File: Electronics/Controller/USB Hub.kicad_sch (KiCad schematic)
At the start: 4 parts, among them J14 MASTER TABLET

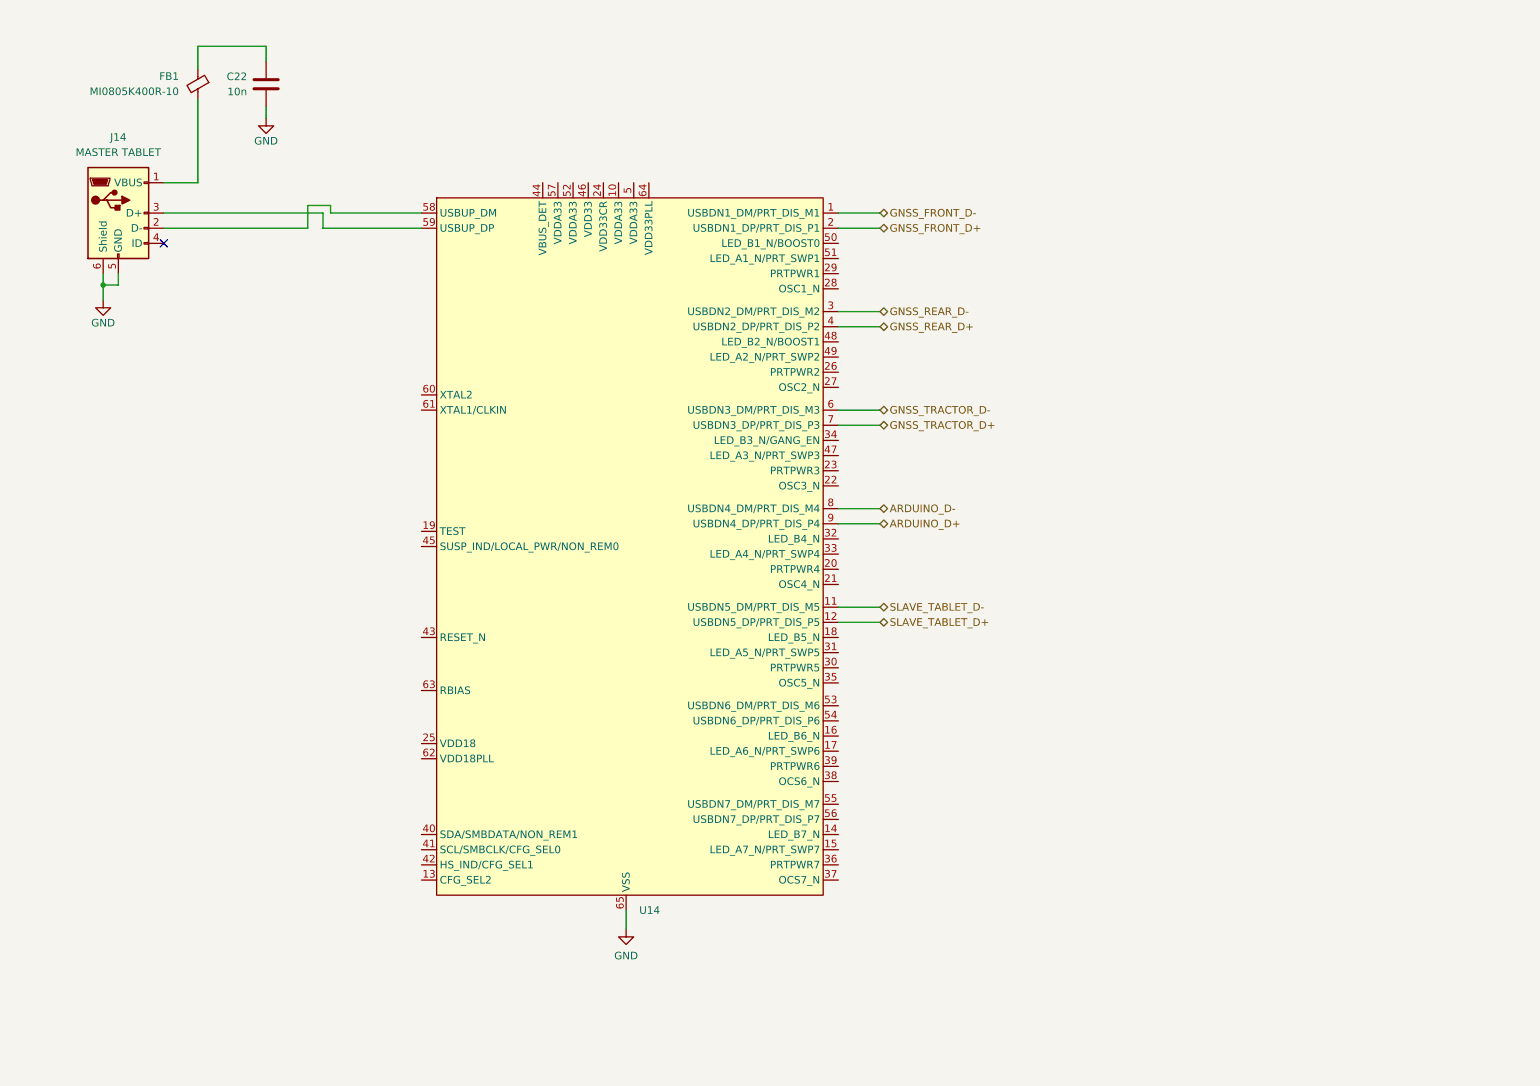
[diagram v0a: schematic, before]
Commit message: Working on schematic. Added datasheets.
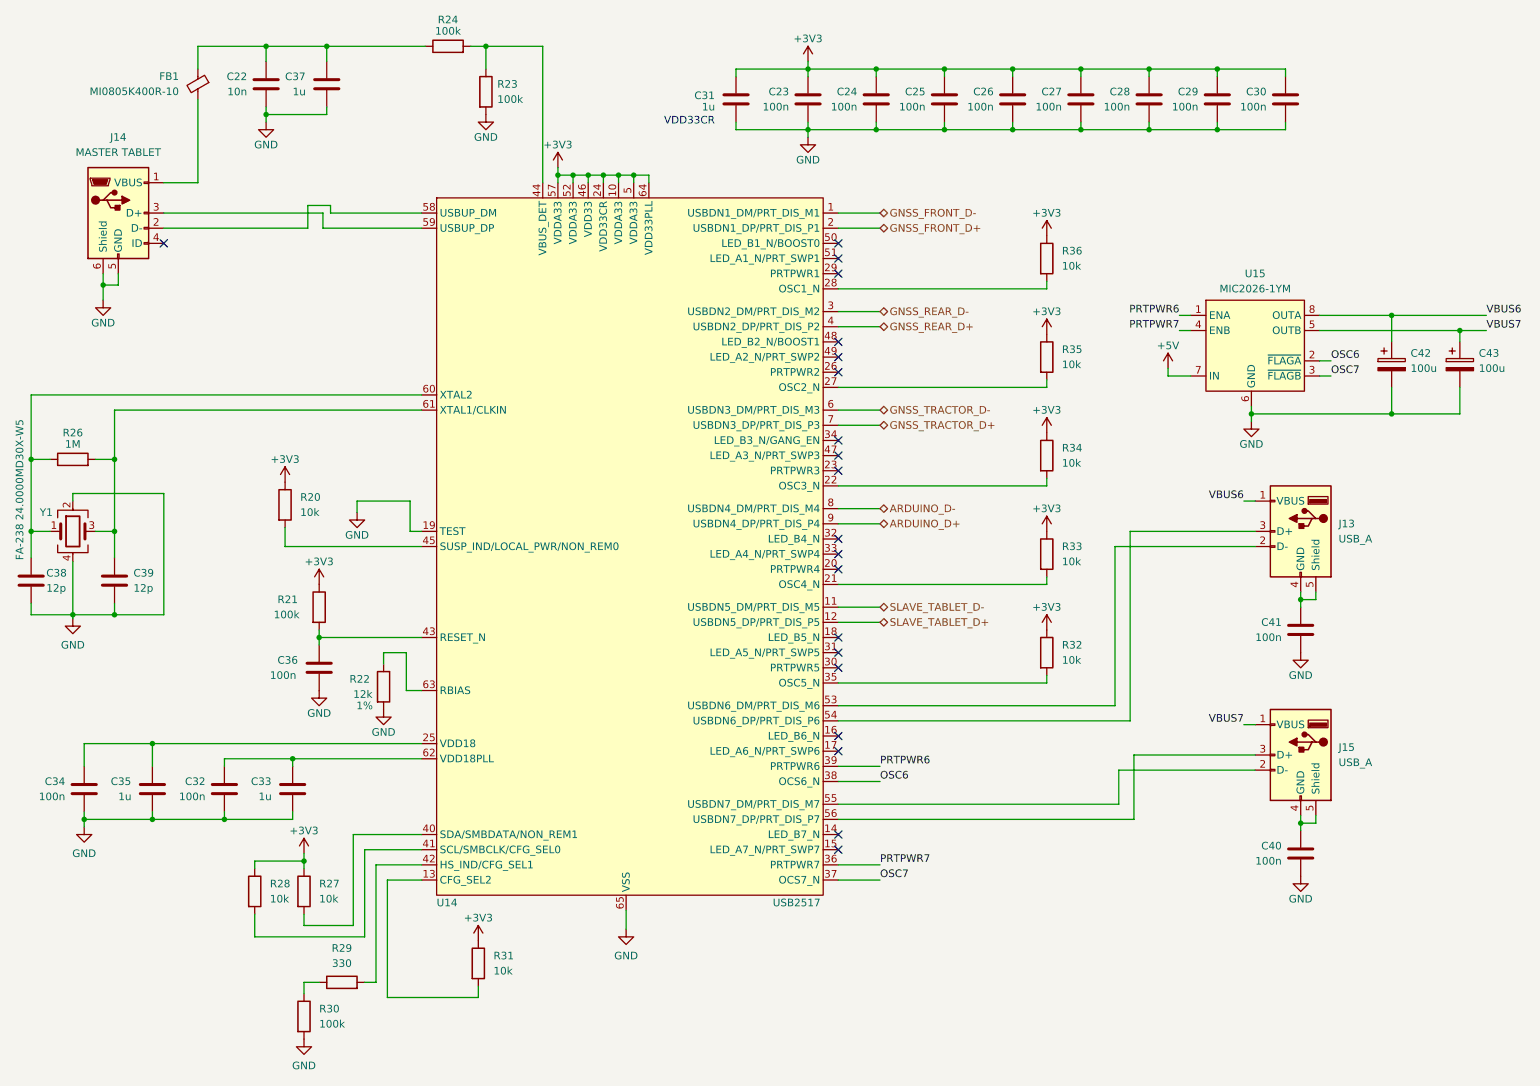
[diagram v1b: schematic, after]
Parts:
- added C23, C24, C25, C26, C27, C28, C29, C30, C32, C34, C36, C40, C41: 100n, symbol Device:C
- added C31, C33, C35, C37: 1u, symbol Device:C
- added C38, C39: 12p, symbol Device:C
- added C42, C43: 100u, symbol Device:C_Polarized
- added J13, J15: USB_A, symbol Connector:USB_A
- added R20, R27, R28, R31, R32, R33, R34, R35, R36: 10k, symbol Device:R
- added R21, R23, R24, R30: 100k, symbol Device:R
- added R22: 12k, symbol Device:R
- added R26: 1M, symbol Device:R
- added R29: 330, symbol Device:R
- added U15: MIC2026-1YM, Package_SO:SOIC-8_3.9x4.9mm_P1.27mm, symbol BritishIdeas2:MIC2026-1YM
- added Y1: FA-238 24.0000MD30X-W5, EmSA:FA-238, symbol Device:Crystal_GND24
- U14: value ~ -> USB2517
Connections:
- net GND: now also U14.19 (TEST), C23.2, C24.2, C25.2, C26.2, C27.2, C28.2, C29.2, C30.2, C31.2, C32.2, C33.2, C34.2, C35.2, C36.2, C37.2, C38.2, C39.2, C40.2, C41.2, C42.2, C43.2, R22.2, R23.2, R30.2, U15.6 (GND), Y1.2, Y1.4
- net at C22.1, FB1.1: now also C37.1, R24.1
- net +3V3: now reaches U14.10 (VDDA33)
- net +3V3: now also U14.24 (VDD33CR), U14.46 (VDD33), U14.5 (VDDA33), U14.52 (VDDA33), U14.57 (VDDA33), U14.64 (VDD33PLL), C23.1, C24.1, C25.1, C26.1, C27.1, C28.1, C29.1, C30.1, C31.1, R20.1, R21.1, R27.1, R28.1, R31.1, R32.1, R33.1, R34.1, R35.1, R36.1
- net at U14.13 (CFG_SEL2): now also R31.2
- net at U14.21 (OSC4_N): now also R33.2
- net at U14.22 (OSC3_N): now also R34.2
- net at U14.25 (VDD18): now also C34.1, C35.1
- net at U14.27 (OSC2_N): now also R35.2
- net at U14.28 (OSC1_N): now also R36.2
- net at U14.35 (OSC5_N): now also R32.2
- net PRTPWR7: now reaches U14.36 (PRTPWR7)
- net PRTPWR7: now also U15.4 (ENB)
- net OSC7: now reaches U14.37 (OCS7_N)
- net OSC7: now also U15.3 (~{FLAGB})
- net OSC6: now reaches U14.38 (OCS6_N)
- net OSC6: now also U15.2 (~{FLAGA})
- net PRTPWR6: now reaches U14.39 (PRTPWR6)
- net PRTPWR6: now also U15.1 (ENA)
- net at U14.40 (SDA/SMBDATA/NON_REM1): now also R27.2
- net at U14.41 (SCL/SMBCLK/CFG_SEL0): now also R28.2
- net at U14.42 (HS_IND/CFG_SEL1): now also R29.2
- net at U14.43 (RESET_N): now also C36.1, R21.2
- net at U14.44 (VBUS_DET): now also R23.1, R24.2
- net at U14.45 (SUSP_IND/LOCAL_PWR/NON_REM0): now also R20.2
- net at U14.53 (USBDN6_DM/PRT_DIS_M6): now also J13.2 (D-)
- net at U14.54 (USBDN6_DP/PRT_DIS_P6): now also J13.3 (D+)
- net at U14.55 (USBDN7_DM/PRT_DIS_M7): now also J15.2 (D-)
- net at U14.56 (USBDN7_DP/PRT_DIS_P7): now also J15.3 (D+)
- net at U14.60 (XTAL2): now also C38.1, R26.1, Y1.1
- net at U14.61 (XTAL1/CLKIN): now also C39.1, R26.2, Y1.3
- net at U14.62 (VDD18PLL): now also C32.1, C33.1
- net at U14.63 (RBIAS): now also R22.1
- new net: C40.1, J15.4 (GND), J15.5 (Shield)
- new net: R29.1, R30.1
- new net: C41.1, J13.4 (GND), J13.5 (Shield)
- new net +5V: U15.7 (IN)
- new net VBUS6: C42.1, J13.1 (VBUS), U15.8 (OUTA)
- new net VBUS7: C43.1, J15.1 (VBUS), U15.5 (OUTB)
- no-connect marks 1 -> 20
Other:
- note added: "VDD33CR"

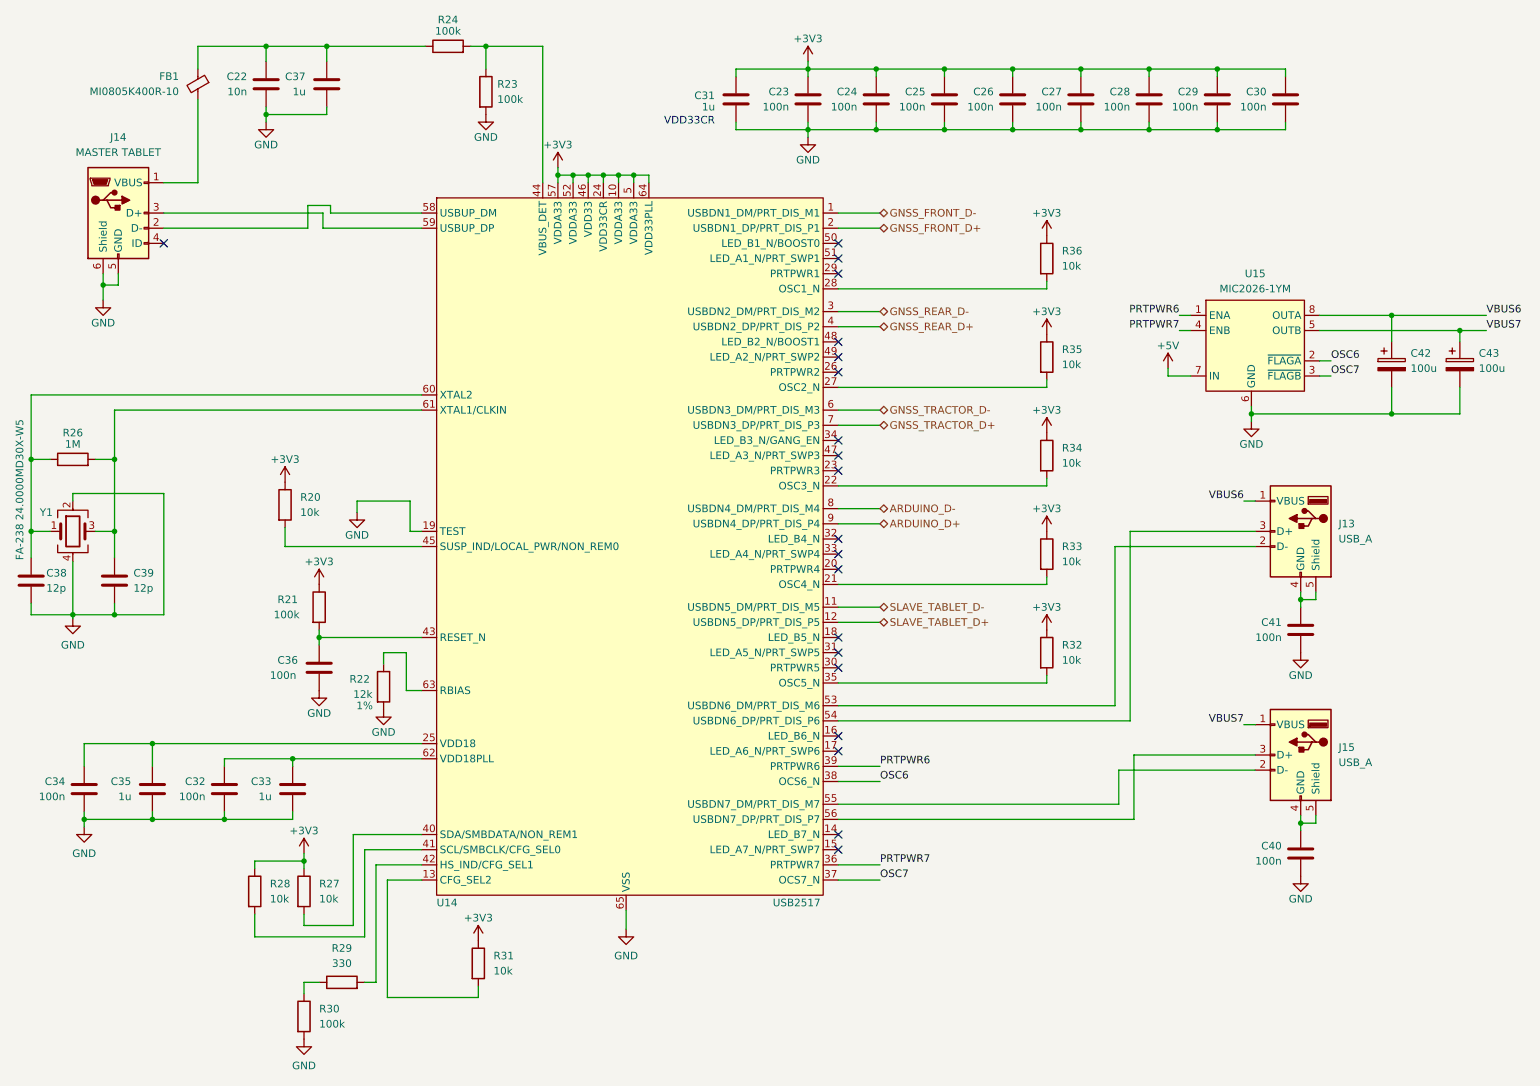
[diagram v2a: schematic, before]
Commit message: Updated schematic. Added footprints for all components.
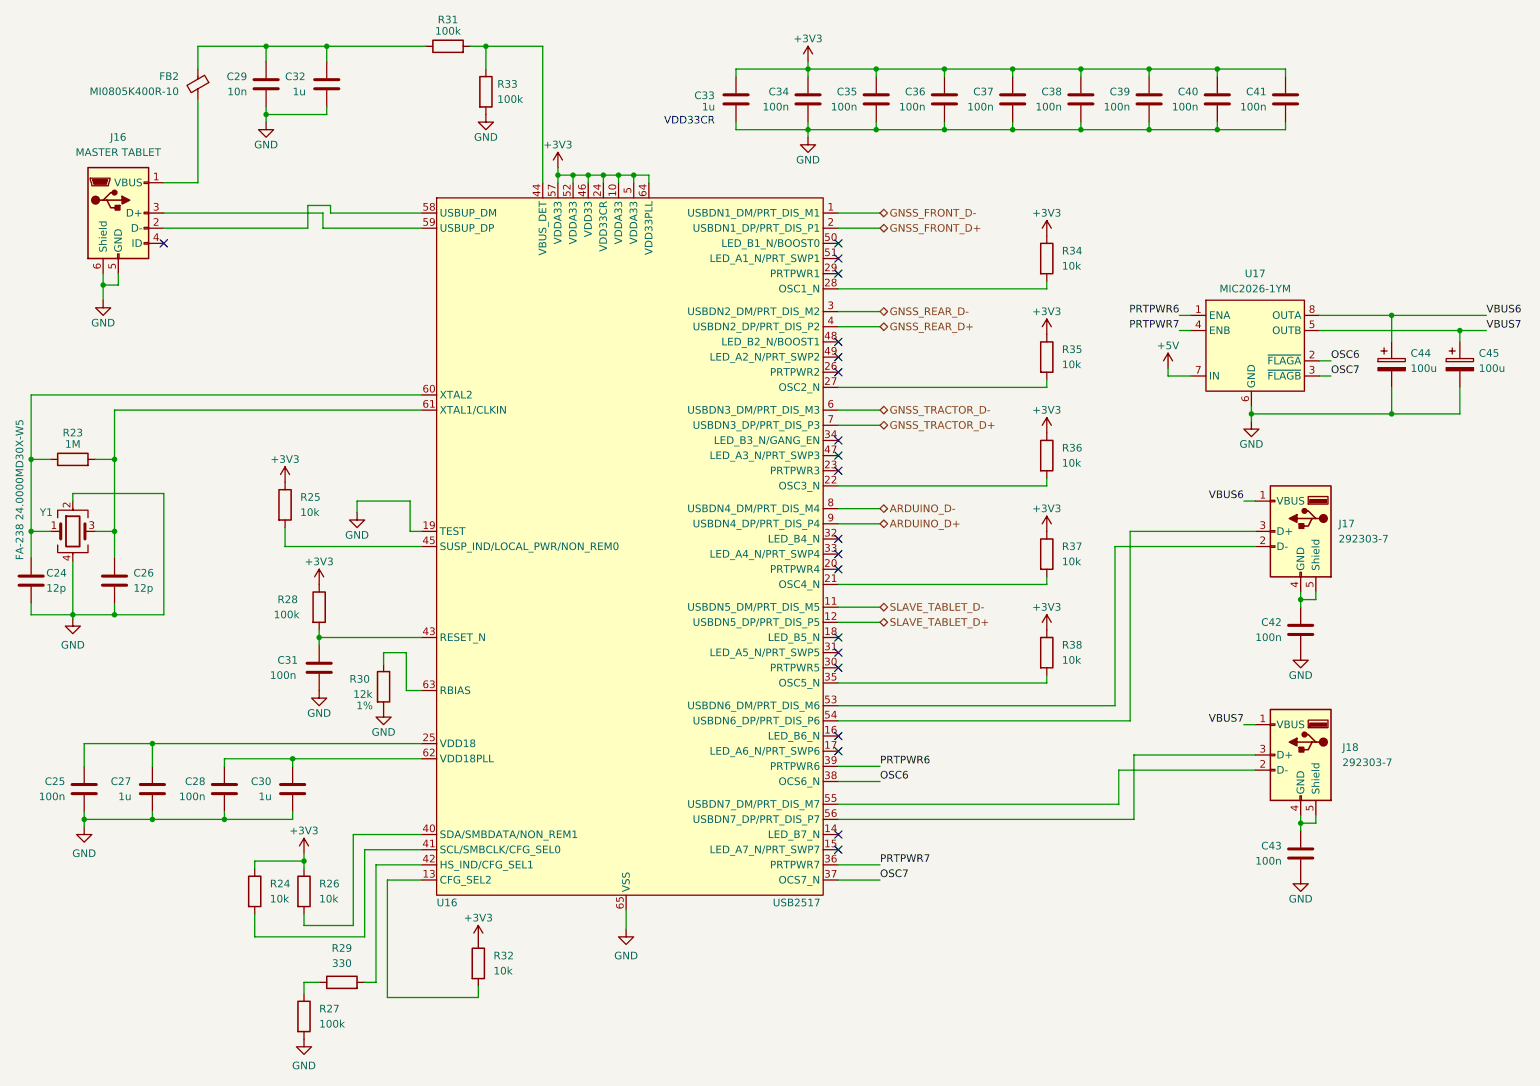
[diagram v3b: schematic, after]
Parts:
- C24: renamed from C38; footprint (none) -> Capacitor_SMD:C_0805_2012Metric
- C25: renamed from C34; footprint (none) -> Capacitor_SMD:C_0805_2012Metric
- C26: renamed from C39; footprint (none) -> Capacitor_SMD:C_0805_2012Metric
- C27: renamed from C35; footprint (none) -> Capacitor_SMD:C_0805_2012Metric
- C28: renamed from C32; footprint (none) -> Capacitor_SMD:C_0805_2012Metric
- C29: renamed from C22; footprint (none) -> Capacitor_SMD:C_0805_2012Metric
- C30: renamed from C33; footprint (none) -> Capacitor_SMD:C_0805_2012Metric
- C31: renamed from C36; footprint (none) -> Capacitor_SMD:C_0805_2012Metric
- C32: renamed from C37; footprint (none) -> Capacitor_SMD:C_0805_2012Metric
- C33: renamed from C31; footprint (none) -> Capacitor_SMD:C_0805_2012Metric
- C34: renamed from C23; footprint (none) -> Capacitor_SMD:C_0805_2012Metric
- C35: renamed from C24; footprint (none) -> Capacitor_SMD:C_0805_2012Metric
- C36: renamed from C25; footprint (none) -> Capacitor_SMD:C_0805_2012Metric
- C37: renamed from C26; footprint (none) -> Capacitor_SMD:C_0805_2012Metric
- C38: renamed from C27; footprint (none) -> Capacitor_SMD:C_0805_2012Metric
- C39: renamed from C28; footprint (none) -> Capacitor_SMD:C_0805_2012Metric
- C40: renamed from C29; footprint (none) -> Capacitor_SMD:C_0805_2012Metric
- C41: renamed from C30; footprint (none) -> Capacitor_SMD:C_0805_2012Metric
- C42: renamed from C41; footprint (none) -> Capacitor_SMD:C_0805_2012Metric
- C43: renamed from C40; footprint (none) -> Capacitor_SMD:C_0805_2012Metric
- C44: renamed from C42; footprint (none) -> Capacitor_SMD:CP_Elec_6.3x5.9; manf# (none) -> UUD1C101MCL1GS
- C45: renamed from C43; footprint (none) -> Capacitor_SMD:CP_Elec_6.3x5.9; manf# (none) -> UUD1C101MCL1GS
- J16: renamed from J14; footprint (none) -> Connector_USB:USB_Micro-B_Amphenol_10103594-0001LF_Horizontal; manf# (none) -> 10103594-0001LF
- J17: renamed from J13; value USB_A -> 292303-7; footprint (none) -> Connector_USB:USB_A_TE_292303-7_Horizontal
- J18: renamed from J15; value USB_A -> 292303-7; footprint (none) -> Connector_USB:USB_A_TE_292303-7_Horizontal
- R23: renamed from R26; footprint (none) -> Resistor_SMD:R_0805_2012Metric
- R24: renamed from R28; footprint (none) -> Resistor_SMD:R_0805_2012Metric
- R25: renamed from R20; footprint (none) -> Resistor_SMD:R_0805_2012Metric
- R26: renamed from R27; footprint (none) -> Resistor_SMD:R_0805_2012Metric
- R27: renamed from R30; footprint (none) -> Resistor_SMD:R_0805_2012Metric
- R28: renamed from R21; footprint (none) -> Resistor_SMD:R_0805_2012Metric
- R29, R35: footprint (none) -> Resistor_SMD:R_0805_2012Metric
- R30: renamed from R22; footprint (none) -> Resistor_SMD:R_0805_2012Metric
- R31: renamed from R24; footprint (none) -> Resistor_SMD:R_0805_2012Metric
- R32: renamed from R31; footprint (none) -> Resistor_SMD:R_0805_2012Metric
- R33: renamed from R23; footprint (none) -> Resistor_SMD:R_0805_2012Metric
- R34: renamed from R36; footprint (none) -> Resistor_SMD:R_0805_2012Metric
- R36: renamed from R34; footprint (none) -> Resistor_SMD:R_0805_2012Metric
- R37: renamed from R33; footprint (none) -> Resistor_SMD:R_0805_2012Metric
- R38: renamed from R32; footprint (none) -> Resistor_SMD:R_0805_2012Metric
- renumbered FB1 to FB2, U14 to U16, U15 to U17
